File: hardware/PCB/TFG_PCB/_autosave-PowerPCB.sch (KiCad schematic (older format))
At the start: 52 parts, among them J1 Conn_01x02_Male, J11 Conn_01x02_Male, J13 Conn_01x02_Male, J15 Conn_01x04_Male, J18 Conn_01x02_Male, J19 Conn_01x02_Male, J21 Conn_01x02_Male, J22 Conn_01x02_Male, J23 Conn_01x04_Male, J25 Conn_01x04_Male, J26 Conn_01x04_Male, J28 Conn_01x02_Male, J30 Conn_01x02_Male, J4 Conn_01x04_Male, J6 Conn_01x04_Male, J7 Conn_01x02_Male, J9 Conn_01x04_Male, Q1 IRF540N, Q4 FDD6685, Q6 FDD6685, Q8 2N7002, U2 L78L05_SOT89, U4 TD7590_2, U6 TD7590_2

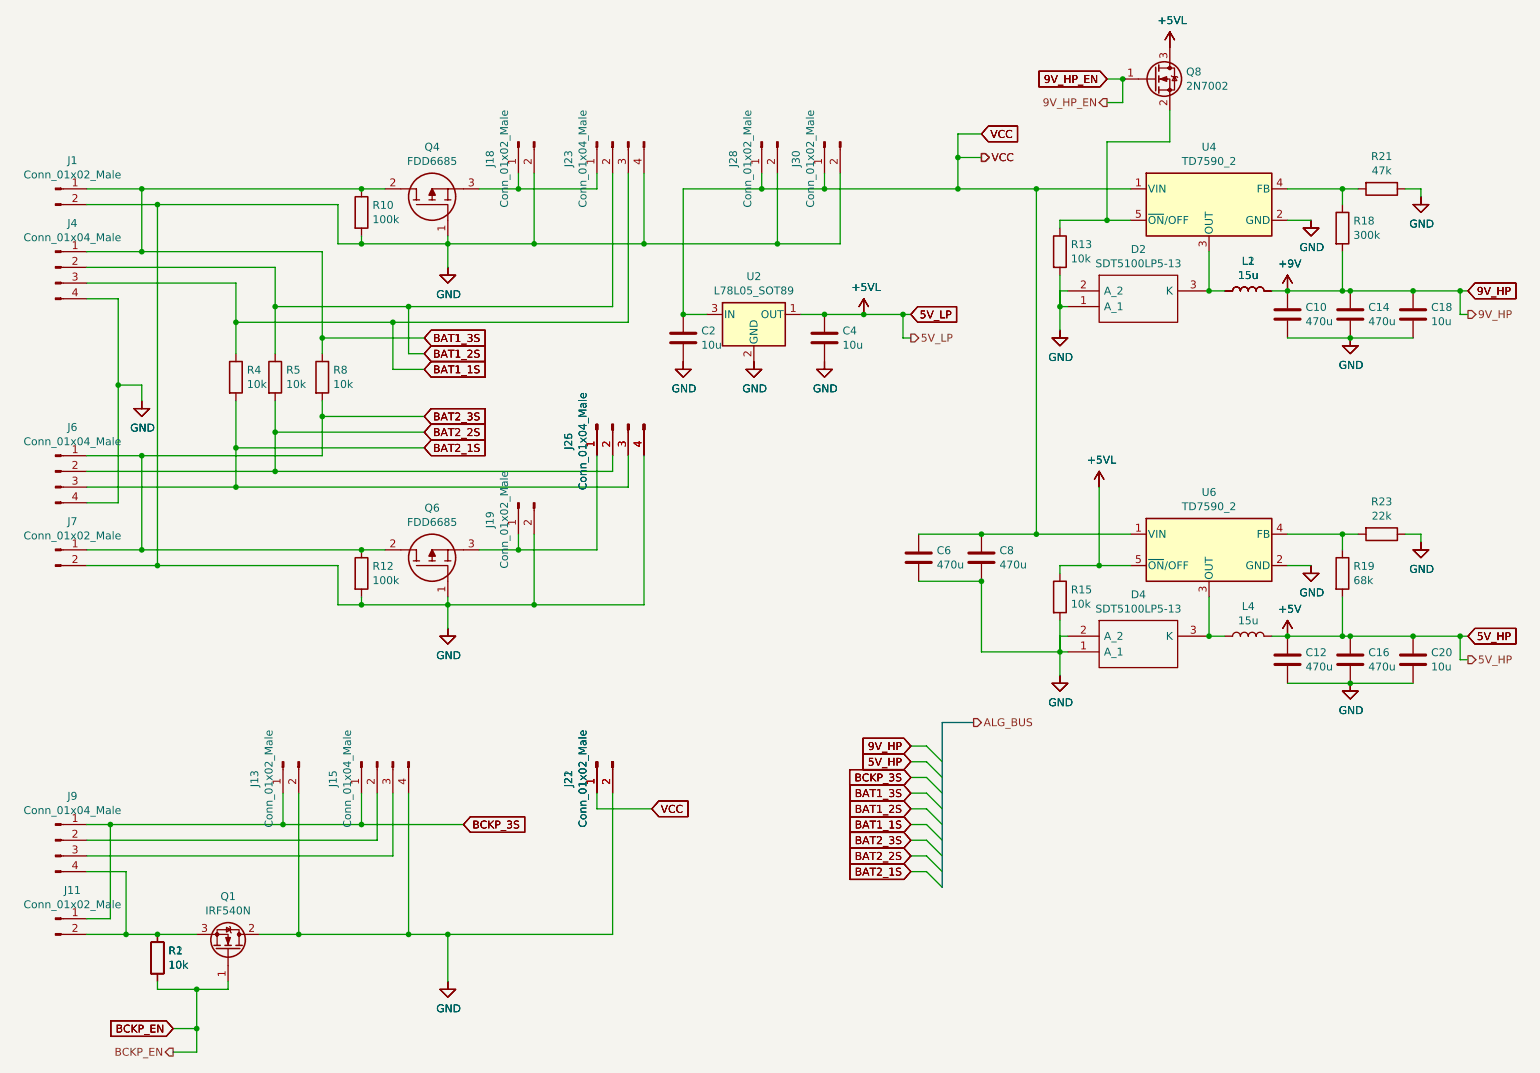
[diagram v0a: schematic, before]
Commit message: Added 40pin GPIO control circuitry
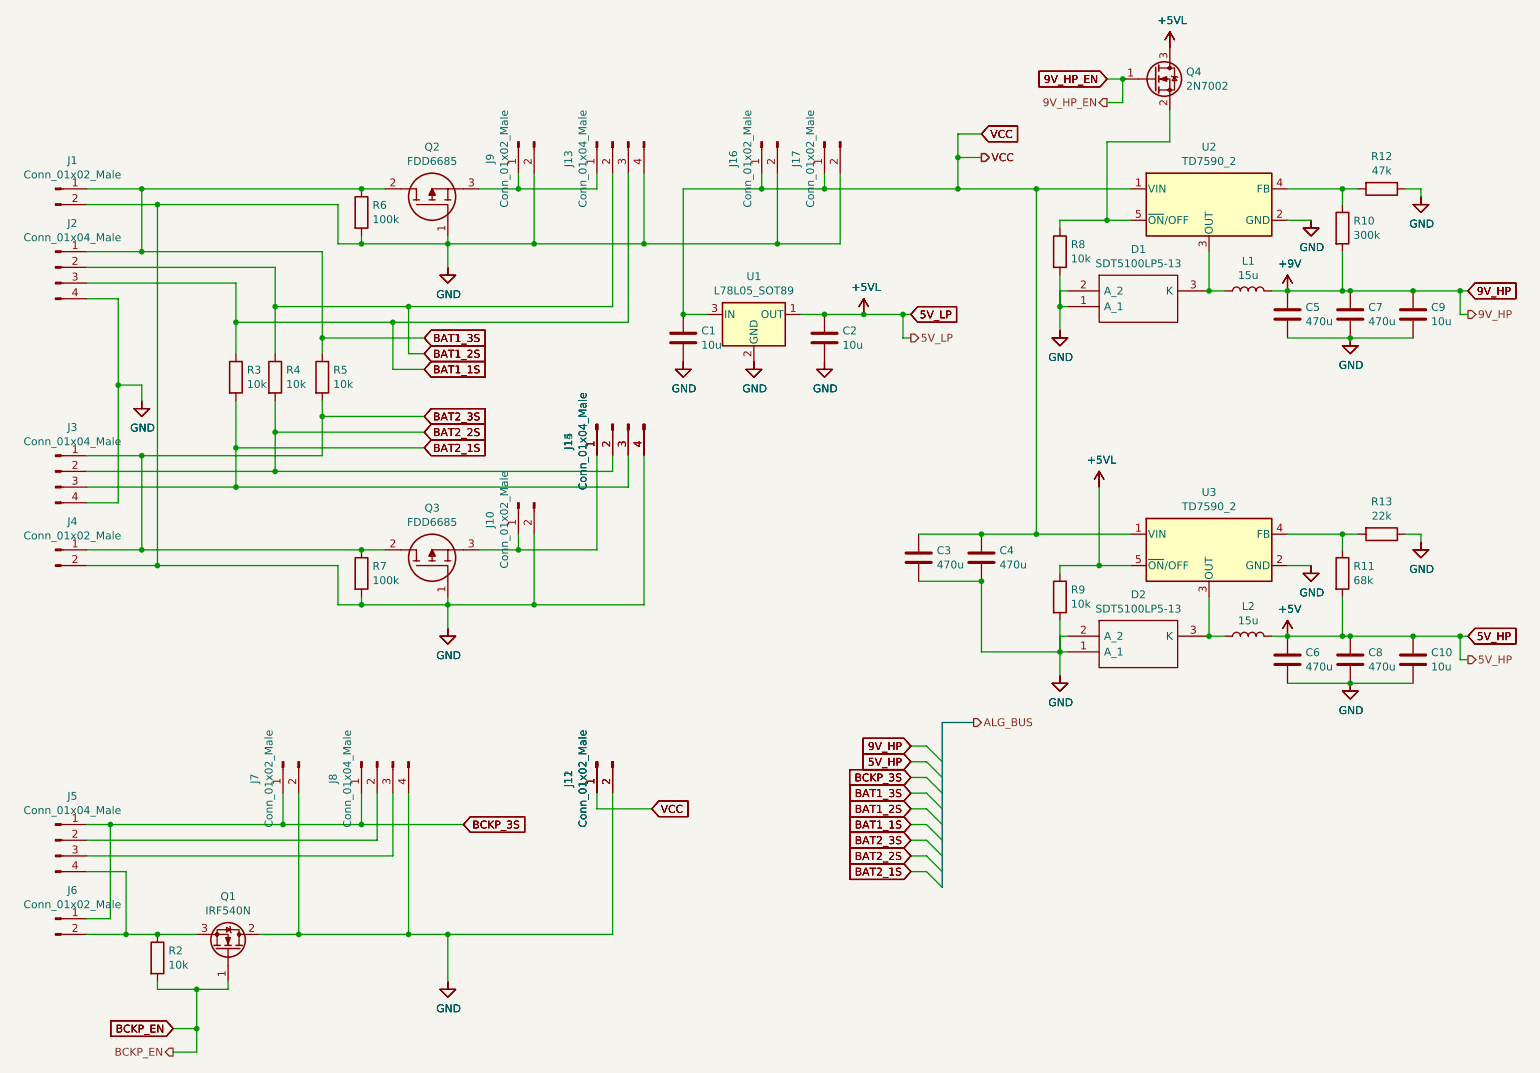
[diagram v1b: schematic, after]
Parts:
- removed L1: 15u, Inductor_SMD:L_0603_1608Metric, symbol Device:L
- removed R1: 10k, symbol Device:R
- renumbered C2 to C1, C20 to C10, C4 to C2, C6 to C3, C8 to C4, C10 to C5, C12 to C6, C14 to C7, C16 to C8, C18 to C9, D2 to D1, D4 to D2, J19 to J10, J21 to J11, J22 to J12, J23 to J13, J25 to J14, J26 to J15, J28 to J16, J30 to J17, J4 to J2, J6 to J3, J7 to J4, J9 to J5, J11 to J6, J13 to J7, J15 to J8, J18 to J9, L2 to L1, L4 to L2, Q4 to Q2, Q6 to Q3, Q8 to Q4, R18 to R10, R19 to R11, R21 to R12, R23 to R13, R4 to R3, R5 to R4, R8 to R5, R10 to R6, R12 to R7, R13 to R8, R15 to R9, U2 to U1, U4 to U2, U6 to U3
